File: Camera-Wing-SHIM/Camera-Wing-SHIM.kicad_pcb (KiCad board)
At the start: 2 copper layers, 21.6 x 52.1 mm, 4 parts, among them J1 Pico RHS Headers, J2 Pin Connection, J3 JST Connection

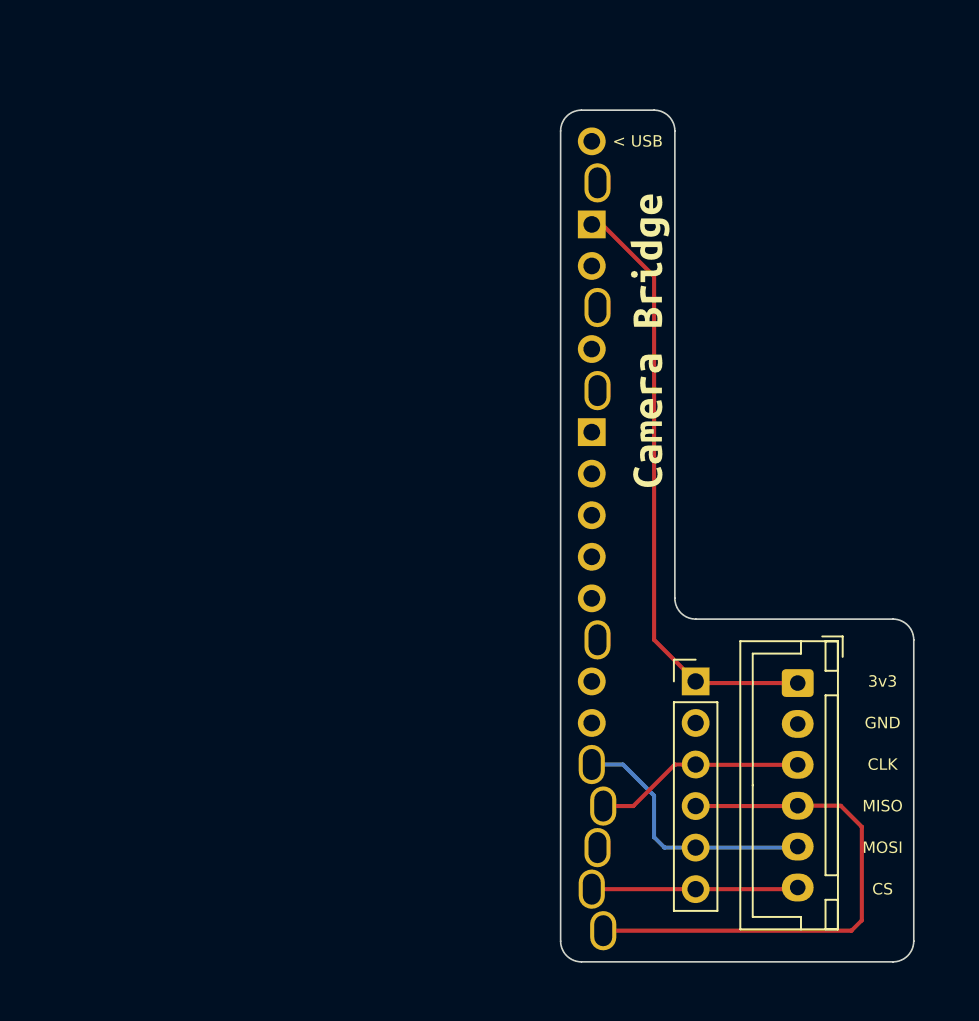
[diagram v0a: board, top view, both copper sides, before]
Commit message: Moved to SMD header
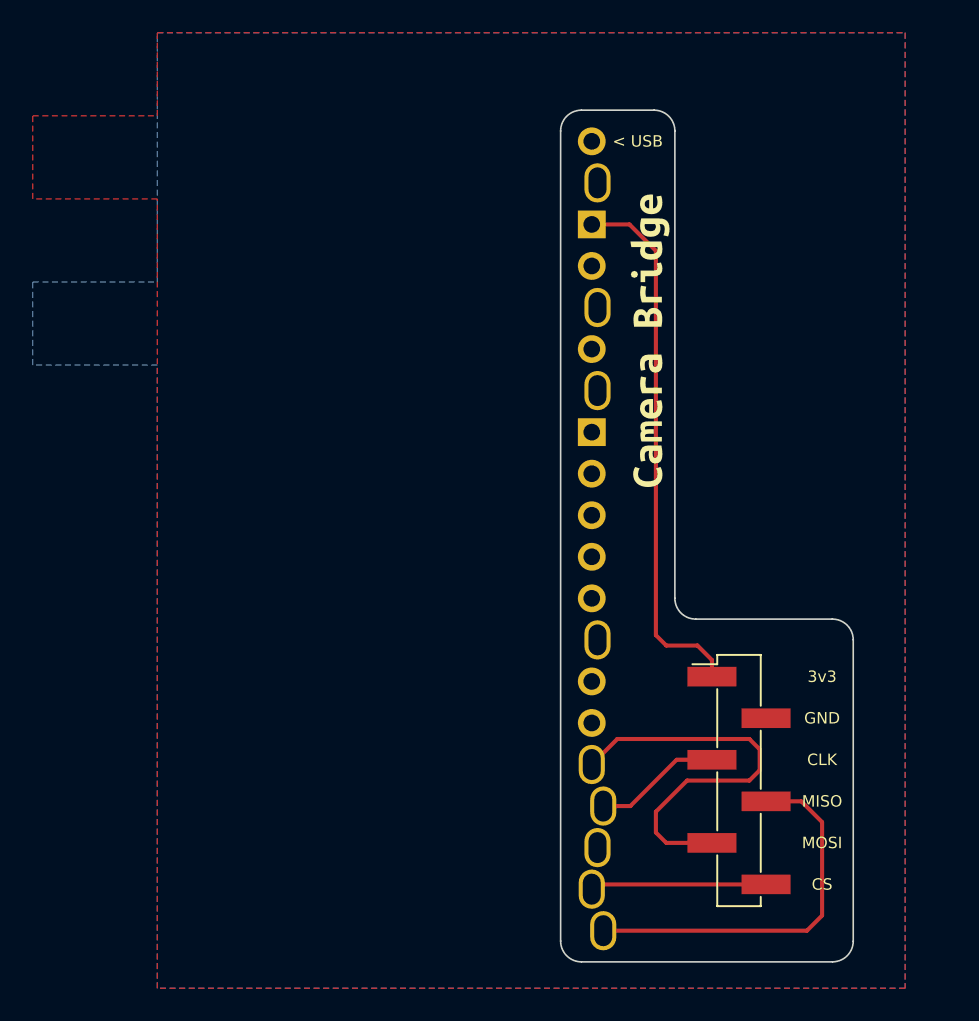
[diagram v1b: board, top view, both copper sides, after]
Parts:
- removed J3: JST Connection, Connector_JST:JST_XH_B6B-XH-A_1x06_P2.50mm_Vertical
- J2: footprint Connector_PinHeader_2.54mm:PinHeader_1x06_P2.54mm_Vertical -> Liam-Footprints:6-pin-SMD-R2
- moved J2 2.83 mm to (90.3, 114.0)
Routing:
- net /MISO: track 32.5 -> 23.4 mm
- net /MOSI: track 16.2 -> 24.8 mm
- net /CLK: track 13.0 -> 7.82 mm
- net +3V3: track 37.2 -> 33.2 mm
- net /CS: track 12.6 -> 10.8 mm
- added copper zone on F.Cu, net (none)
- added copper zone on B.Cu, net GND
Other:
- board size 21.6 x 52.1 mm -> 17.9 x 52.1 mm

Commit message: Fixed
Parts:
- removed kibuzzard-6576E9F4: G***, kibuzzard-6576E9F4
- added G***: LOGO, Artwork:camera-art, B.Cu at (94.4, 116.5)
- added J3: Pin Connection, Connector_PinHeader_2.54mm:PinHeader_1x06_P2.54mm_Vertical, F.Cu at (87.8, 113.0)
- added kibuzzard-65ACBA76: G***, kibuzzard-65ACBA76, F.Cu at (84.7, 94.7)
- J2: value Pin Connection -> SMD Header Connection
- moved J2 3.57 mm to (93.9, 114.3)
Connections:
- J1 pad 3: +3V3 -> GND
- J1 pad 5: GND -> +3V3
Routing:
- net /MOSI: track 24.8 -> 13.0 mm
- net GND: track 0.00 -> 7.75 mm
- net /MISO: track 23.4 -> 18.5 mm
- net /CS: track 10.8 -> 14.2 mm
- net /CLK: track 7.82 -> 11.3 mm
- net +3V3: track 33.2 -> 31.9 mm
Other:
- board size 17.9 x 52.1 mm -> 22.3 x 52.1 mm
- board text added: "Mega SPI Camera"
- board text added: "USB>"
- board text removed: "< USB"
